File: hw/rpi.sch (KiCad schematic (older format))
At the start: 9 parts

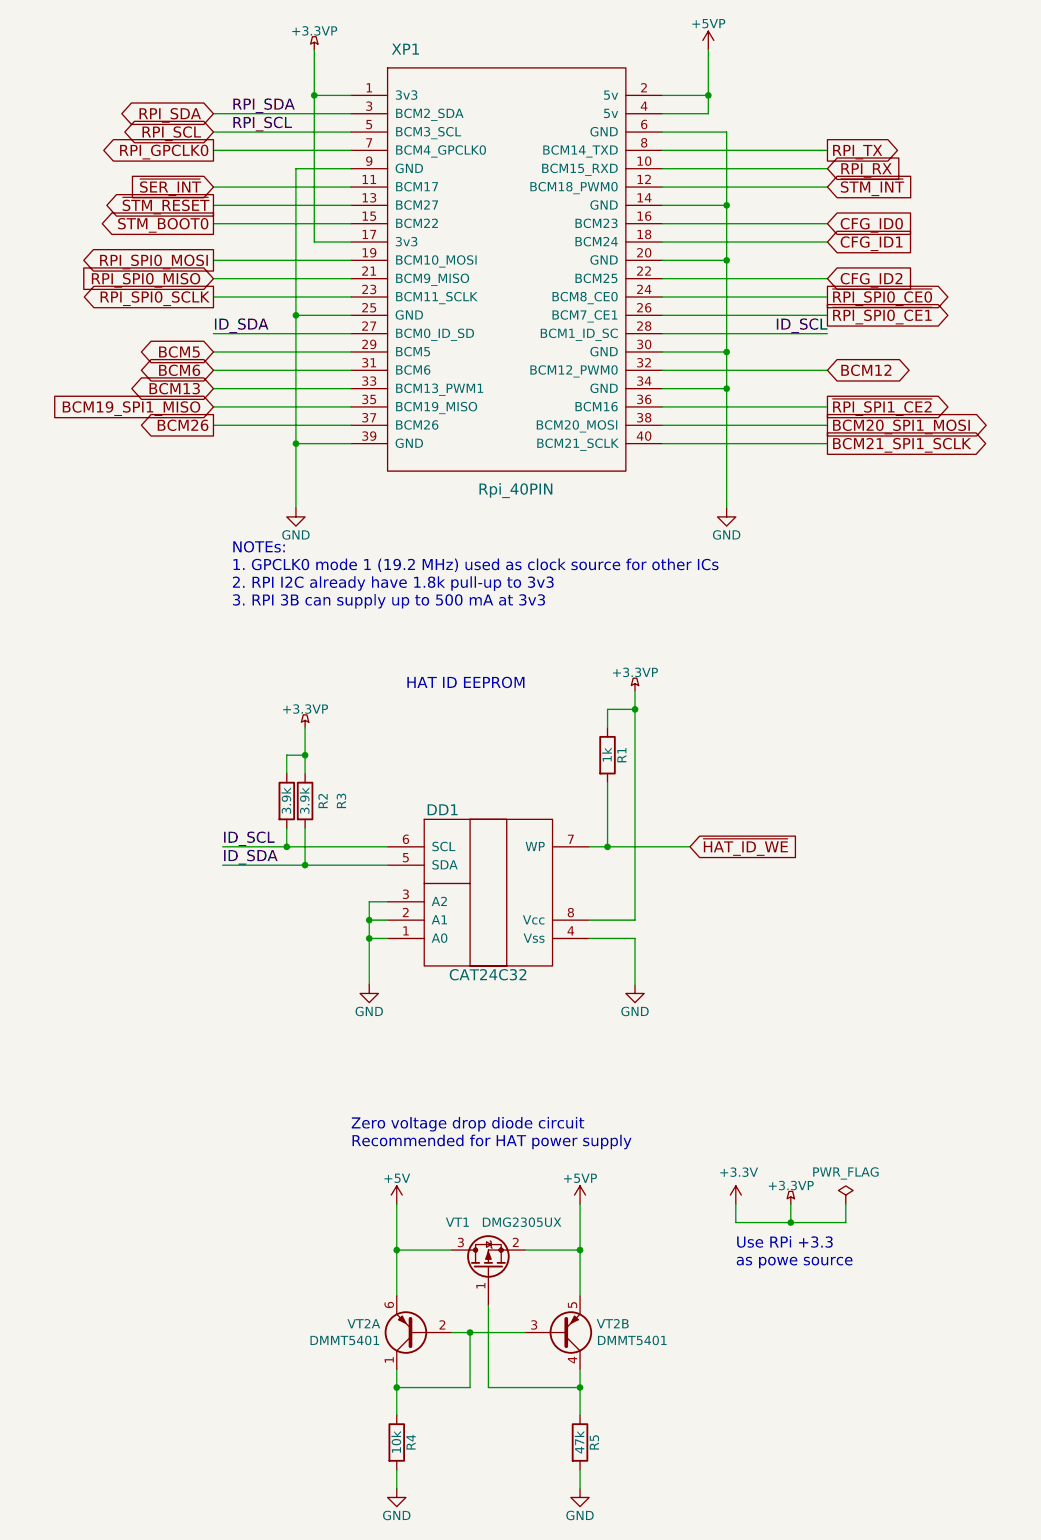
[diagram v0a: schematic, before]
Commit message: hw: fix ERC
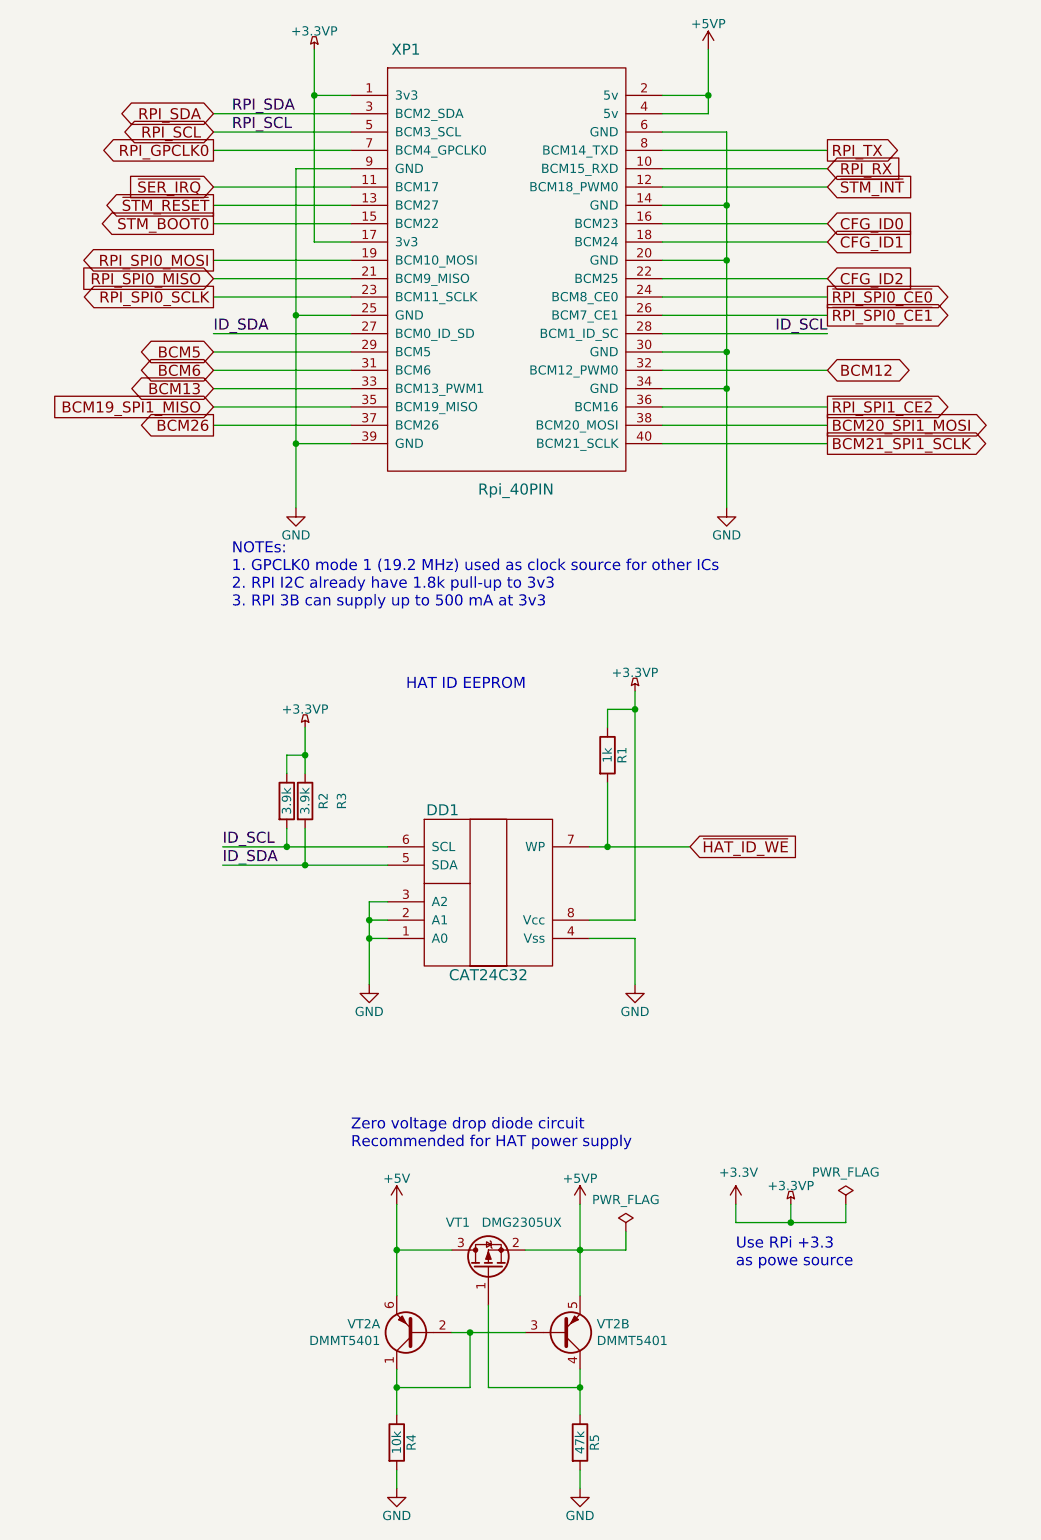
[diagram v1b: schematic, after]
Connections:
- net ~SER_INT renamed ~SER_IRQ
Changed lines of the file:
@@
 NOTEs:\n1. GPCLK0 mode 1 (19.2 MHz) used as clock source for other ICs\n2. RPI I2C already have 1.8k pull-up to 3v3\n3. RPI 3B can supply up to 500 mA at 3v3
 Text GLabel 2800 2450 0    60   Input ~ 0
-~SER_INT
+~SER_IRQ
 Wire Wire Line
 	2800 2450 3550 2450
@@
 	1    0    0    1
 $EndComp
+$Comp
+L power:PWR_FLAG #FLG0102
+U 1 1 5AE4F91B
+P 5050 8150
+F 0 "#FLG0102" H 5050 8225 50  0001 C CNN
+F 1 "PWR_FLAG" H 5050 8324 50  0000 C CNN
+F 2 "" H 5050 8150 50  0001 C CNN
+F 3 "" H 5050 8150 50  0001 C CNN
+	1    5050 8150
+	1    0    0    -1
+$EndComp
+Wire Wire Line
+	4800 8250 5050 8250
+Wire Wire Line
+	5050 8250 5050 8150
 $EndSCHEMATC

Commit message: hw: cvpcb for R,C
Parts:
- DD1: footprint (none) -> Package_SO:SO-8_5.3x6.2mm_P1.27mm
- R1, R2, R3, R4, R5: footprint (none) -> Resistor_SMD:R_0603_1608Metric
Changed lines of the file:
@@
 F 0 "DD1" H 4050 6750 60  0000 C CNN
 F 1 "CAT24C32" H 4300 5850 60  0000 C CNN
-F 2 "" V 2700 7750 60  0001 C CNN
+F 2 "Package_SO:SO-8_5.3x6.2mm_P1.27mm" V 2700 7750 60  0001 C CNN
 F 3 "" V 2700 7750 60  0001 C CNN
 	1    4300 6300
@@
 ID_SCL
 $Comp
-L power:GND #PWR05
+L power:GND #PWR08
 U 1 1 5AB011CD
 P 5100 6800
-F 0 "#PWR05" H 5100 6550 50  0001 C CNN
+F 0 "#PWR08" H 5100 6550 50  0001 C CNN
 F 1 "GND" H 5100 6650 50  0000 C CNN
 F 2 "" H 5100 6800 50  0001 C CNN
@@
 $EndComp
 $Comp
-L power:+3.3VP #PWR06
+L power:+3.3VP #PWR05
 U 1 1 5AB01486
 P 5100 5200
-F 0 "#PWR06" H 5250 5150 50  0001 C CNN
+F 0 "#PWR05" H 5250 5150 50  0001 C CNN
 F 1 "+3.3VP" H 5100 5300 50  0000 C CNN
 F 2 "" H 5100 5200 50  0001 C CNN
@@
 F 0 "R1" V 5030 5550 50  0000 C CNN
 F 1 "1k" V 4950 5550 50  0000 C CNN
-F 2 "" V 4880 5550 50  0001 C CNN
+F 2 "Resistor_SMD:R_0603_1608Metric" V 4880 5550 50  0001 C CNN
 F 3 "" H 4950 5550 50  0001 C CNN
 	1    4950 5550
@@
 F 0 "R2" V 3400 5800 50  0000 C CNN
 F 1 "3.9k" V 3200 5800 50  0000 C CNN
-F 2 "" V 3130 5800 50  0001 C CNN
+F 2 "Resistor_SMD:R_0603_1608Metric" V 3130 5800 50  0001 C CNN
 F 3 "" H 3200 5800 50  0001 C CNN
 	1    3200 5800
@@
 F 0 "R3" V 3500 5800 50  0000 C CNN
 F 1 "3.9k" V 3300 5800 50  0000 C CNN
-F 2 "" V 3230 5800 50  0001 C CNN
+F 2 "Resistor_SMD:R_0603_1608Metric" V 3230 5800 50  0001 C CNN
 F 3 "" H 3300 5800 50  0001 C CNN
 	1    3300 5800
@@
 $EndComp
 $Comp
-L power:+3.3VP #PWR07
+L power:+3.3VP #PWR06
 U 1 1 5AB01EB8
 P 3300 5400
-F 0 "#PWR07" H 3450 5350 50  0001 C CNN
+F 0 "#PWR06" H 3450 5350 50  0001 C CNN
 F 1 "+3.3VP" H 3300 5500 50  0000 C CNN
 F 2 "" H 3300 5400 50  0001 C CNN
@@
 ID_SDA
 $Comp
-L power:GND #PWR08
+L power:GND #PWR07
 U 1 1 5AB0290A
 P 3650 6800
-F 0 "#PWR08" H 3650 6550 50  0001 C CNN
+F 0 "#PWR07" H 3650 6550 50  0001 C CNN
 F 1 "GND" H 3650 6650 50  0000 C CNN
 F 2 "" H 3650 6800 50  0001 C CNN
@@
 Connection ~ 3800 9000
 $Comp
-L power:GND #PWR09
+L power:GND #PWR014
 U 1 1 5AB1380A
 P 4800 9550
-F 0 "#PWR09" H 4800 9300 50  0001 C CNN
+F 0 "#PWR014" H 4800 9300 50  0001 C CNN
 F 1 "GND" H 4800 9400 50  0000 C CNN
 F 2 "" H 4800 9550 50  0001 C CNN
@@
 F 0 "R5" V 4880 9300 50  0000 C CNN
 F 1 "47k" V 4800 9300 50  0000 C CNN
-F 2 "" V 4730 9300 50  0001 C CNN
+F 2 "Resistor_SMD:R_0603_1608Metric" V 4730 9300 50  0001 C CNN
 F 3 "" H 4800 9300 50  0001 C CNN
 	1    4800 9300
@@
 F 0 "R4" V 3880 9300 50  0000 C CNN
 F 1 "10k" V 3800 9300 50  0000 C CNN
-F 2 "" V 3730 9300 50  0001 C CNN
+F 2 "Resistor_SMD:R_0603_1608Metric" V 3730 9300 50  0001 C CNN
 F 3 "" H 3800 9300 50  0001 C CNN
 	1    3800 9300
@@
 Connection ~ 4200 8700
 $Comp
-L power:GND #PWR010
+L power:GND #PWR013
 U 1 1 5AB1428A
 P 3800 9550
-F 0 "#PWR010" H 3800 9300 50  0001 C CNN
+F 0 "#PWR013" H 3800 9300 50  0001 C CNN
 F 1 "GND" H 3800 9400 50  0000 C CNN
 F 2 "" H 3800 9550 50  0001 C CNN
@@
 	4800 9450 4800 9550
 $Comp
-L power:+5VP #PWR011
+L power:+5VP #PWR010
 U 1 1 5AB14AE1
 P 4800 8000
-F 0 "#PWR011" H 4800 7850 50  0001 C CNN
+F 0 "#PWR010" H 4800 7850 50  0001 C CNN
 F 1 "+5VP" H 4800 8140 50  0000 C CNN
 F 2 "" H 4800 8000 50  0001 C CNN
@@
 $EndComp
 $Comp
-L power:+5V #PWR012
+L power:+5V #PWR09
 U 1 1 5AB1599D
 P 3800 8000
-F 0 "#PWR012" H 3800 7850 50  0001 C CNN
+F 0 "#PWR09" H 3800 7850 50  0001 C CNN
 F 1 "+5V" H 3800 8140 50  0000 C CNN
 F 2 "" H 3800 8000 50  0001 C CNN
@@
 Connection ~ 4950 6050
 $Comp
-L power:+3.3V #PWR013
+L power:+3.3V #PWR011
 U 1 1 5AC14350
 P 5650 8000
-F 0 "#PWR013" H 5650 7850 50  0001 C CNN
+F 0 "#PWR011" H 5650 7850 50  0001 C CNN
 F 1 "+3.3V" H 5665 8173 50  0000 C CNN
 F 2 "" H 5650 8000 50  0001 C CNN
@@
 $EndComp
 $Comp
-L power:+3.3VP #PWR015
+L power:+3.3VP #PWR012
 U 1 1 5AC148A8
 P 5950 8000
-F 0 "#PWR015" H 6100 7950 50  0001 C CNN
+F 0 "#PWR012" H 6100 7950 50  0001 C CNN
 F 1 "+3.3VP" H 5950 8100 50  0000 C CNN
 F 2 "" H 5950 8000 50  0001 C CNN
@@
 $EndComp
 $Comp
-L power:PWR_FLAG #FLG0102
+L power:PWR_FLAG #FLG02
 U 1 1 5AE4F91B
 P 5050 8150
-F 0 "#FLG0102" H 5050 8225 50  0001 C CNN
+F 0 "#FLG02" H 5050 8225 50  0001 C CNN
 F 1 "PWR_FLAG" H 5050 8324 50  0000 C CNN
 F 2 "" H 5050 8150 50  0001 C CNN

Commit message: hw: more cvpcb
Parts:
- DD1: value CAT24C32 -> CAT24C256WI-GT3
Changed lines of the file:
@@
 P 4300 6300
 F 0 "DD1" H 4050 6750 60  0000 C CNN
-F 1 "CAT24C32" H 4300 5850 60  0000 C CNN
+F 1 "CAT24C256WI-GT3" H 4300 5850 60  0000 C CNN
 F 2 "Package_SO:SO-8_5.3x6.2mm_P1.27mm" V 2700 7750 60  0001 C CNN
 F 3 "" V 2700 7750 60  0001 C CNN

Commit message: hw: wonring on NET
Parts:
- VT1: footprint TO_SOT_Packages_SMD:SOT-23_Handsoldering -> Package_TO_SOT_SMD:SOT-23_Handsoldering
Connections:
- net ZVD_G: now reaches R5.1, VT1.1 (G), VT2.4 (C2)
- net ZVD_B: now reaches R4.1, VT2.1 (C1), VT2.2 (B1), VT2.3 (B2)
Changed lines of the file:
@@
 F 0 "VT1" V 4550 8450 50  0000 L CNN
 F 1 "DMG2305UX" V 4550 7950 50  0000 L CNN
-F 2 "TO_SOT_Packages_SMD:SOT-23_Handsoldering" H 4500 8450 50  0001 C CNN
+F 2 "Package_TO_SOT_SMD:SOT-23_Handsoldering" H 4500 8450 50  0001 C CNN
 F 3 "" H 4300 8350 50  0001 C CNN
 	1    4300 8350
@@
 Wire Wire Line
 	5050 8250 5050 8150
+Text Label 3900 9000 0    60   ~ 0
+ZVD_B
+Text Label 4400 9000 0    60   ~ 0
+ZVD_G
 $EndSCHEMATC

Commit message: hw: add 40-pin header mod
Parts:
- XP1: footprint (none) -> hat:RaspberryPi-40Pin_P2.54mm
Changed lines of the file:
@@
 F 0 "XP1" H 3850 4100 60  0000 C CNN
 F 1 "Rpi_40PIN" H 4450 1700 60  0000 C CNN
-F 2 "" H 4050 3000 60  0001 C CNN
+F 2 "hat:RaspberryPi-40Pin_P2.54mm" H 4050 3000 60  0001 C CNN
 F 3 "" H 4050 3000 60  0001 C CNN
 	1    4400 2900

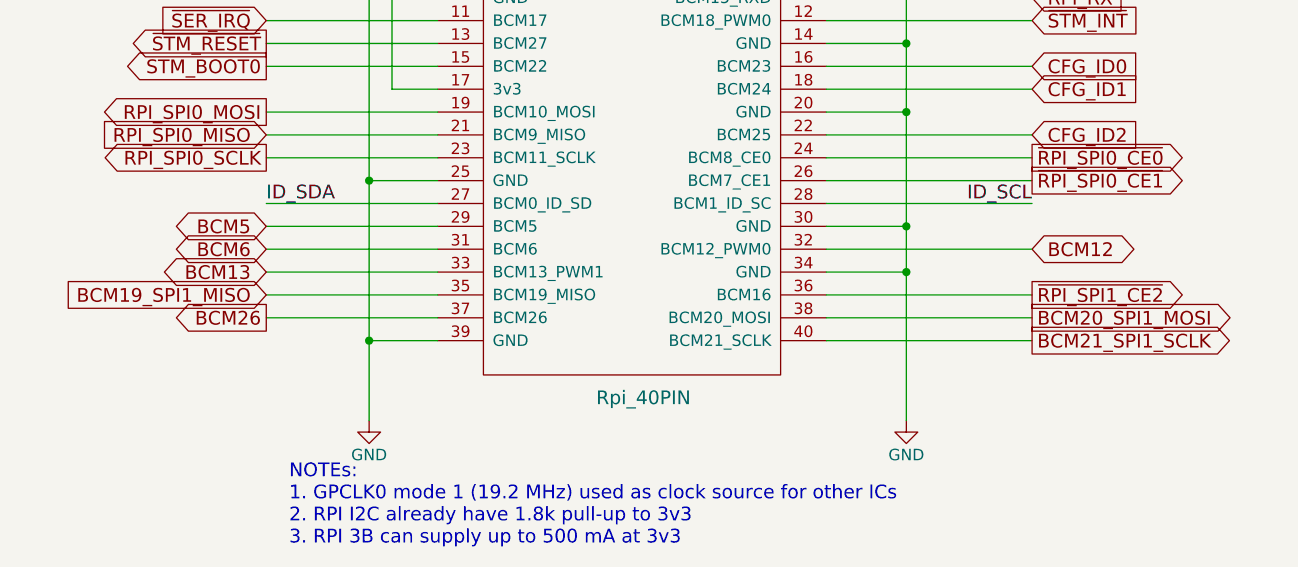
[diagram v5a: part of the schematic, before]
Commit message: hw: remove header with unused rpi gpio's, more net labels
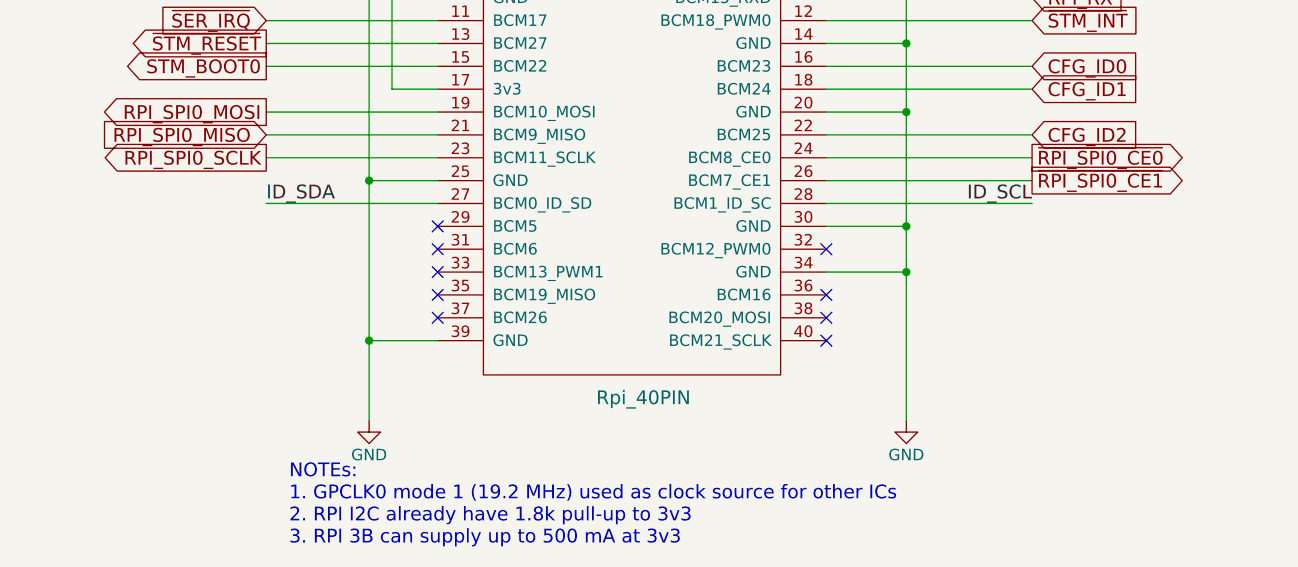
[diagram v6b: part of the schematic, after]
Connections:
- net BCM12: no longer names the net of XP1.32 (BCM12_PWM0)
- net BCM13: no longer names the net of XP1.33 (BCM13_PWM1)
- net BCM19_SPI1_MISO: no longer names the net of XP1.35 (BCM19_MISO)
- net BCM20_SPI1_MOSI: no longer names the net of XP1.38 (BCM20_MOSI)
- net BCM21_SPI1_SCLK: no longer names the net of XP1.40 (BCM21_SCLK)
- net BCM26: no longer names the net of XP1.37 (BCM26)
- net BCM5: no longer names the net of XP1.29 (BCM5)
- net BCM6: no longer names the net of XP1.31 (BCM6)
- net ~RPI_SPI1_CE2: no longer names the net of XP1.36 (BCM16)
- no-connect marks 0 -> 9
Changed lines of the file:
@@
 Wire Wire Line
 	6150 2450 5250 2450
-Text GLabel 6150 3750 2    60   Output ~ 0
-BCM20_SPI1_MOSI
-Text GLabel 6150 3850 2    60   Output ~ 0
-BCM21_SPI1_SCLK
-Text GLabel 6150 3650 2    60   Output ~ 0
-~RPI_SPI1_CE2
-Text GLabel 2800 3650 0    60   Input ~ 0
-BCM19_SPI1_MISO
-Wire Wire Line
-	5250 3650 6150 3650
-Wire Wire Line
-	5250 3750 6150 3750
-Wire Wire Line
-	5250 3850 6150 3850
-Wire Wire Line
-	2800 3650 3550 3650
 Text GLabel 6150 2650 2    60   Input ~ 0
 CFG_ID0
@@
 Wire Wire Line
 	6150 2750 5250 2750
-Text GLabel 2800 3750 0    60   Output ~ 0
-BCM26
-Text GLabel 2800 3550 0    60   BiDi ~ 0
-BCM13
-Wire Wire Line
-	3550 3550 2800 3550
-Wire Wire Line
-	2800 3750 3550 3750
-Text GLabel 2800 3350 0    60   BiDi ~ 0
-BCM5
-Text GLabel 2800 3450 0    60   BiDi ~ 0
-BCM6
-Wire Wire Line
-	2800 3350 3550 3350
-Wire Wire Line
-	3550 3450 2800 3450
-Text GLabel 6150 3450 2    60   BiDi ~ 0
-BCM12
 Text GLabel 6150 2950 2    60   Input ~ 0
 CFG_ID2
 Wire Wire Line
 	6150 2950 5250 2950
-Wire Wire Line
-	5250 3450 6150 3450
 Wire Wire Line
 	3350 1950 3350 2750
@@
 Text Label 4400 9000 0    60   ~ 0
 ZVD_G
+NoConn ~ 3550 3350
+NoConn ~ 3550 3450
+NoConn ~ 3550 3550
+NoConn ~ 3550 3650
+NoConn ~ 3550 3750
+NoConn ~ 5250 3450
+NoConn ~ 5250 3650
+NoConn ~ 5250 3750
+NoConn ~ 5250 3850
 $EndSCHEMATC
